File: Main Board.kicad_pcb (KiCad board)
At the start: 4 copper layers, 161 x 92 mm, 380 parts, among them J1 Motor Y, J10 CA58SUB-B, J11 PC6 EPSON MAINBOARD, J12 Y AXIS, J13 Z AXIS, J14 LED 1, J15 LED 2, J16 Power Input, J17 VS, J18 12V, J19 5V, J2 Motor Z, J20 3.3V, J21 TABLE SENSOR, J22 INPUT1, J23 INPUT2, J24 PHOTO SENSOR EMITER, J25 PHOTO SENSOR RECEIVER, J26 ANALOG, J27 INPUT3, J28 OUT1, J29 OUT2, J3 USB_B, J30 RELAY, J31 EMERGENCY, J32 EPSON POWER IN, J33 EPSON BOARD POWER, J34 Display, J35 SPI Interface, J36 I2C Interface, J37 LED4, J38 LED3, J39 Key 3, J4 SWD, J40 Key 4, J41 Key 1, J42 Key 2, J43 Encoder, J5 DEBUG, J6 LIMIT Y BACK, J7 LIMIT Y FRONT, J8 LIMIT Z UP, J9 LIMIT Z DOWN, K1 S13-24V-2C, Q1 2N7002K, Q10 2N7002K, Q11 BC817, Q12 BC817, Q13 BC817, Q14 2N7002K, Q15 2N7002K, Q16 2N7002K, Q17 BC817, Q18 2N7002K, Q19 2N7002K, Q2 2N7002K, Q20 2N7002K, Q21 2N7002K, Q3 2N7002K, Q4 2N7002K, Q5 2N7002K, Q6 2N7002K, Q7 2N7002K, Q8 YJS9435A, Q9 2N7002K, U1 TMC2209-LA, U10 74HC2G32, U11 74HC245, U12 SHTC3, U2 TMC2209-LA, U3 STM32F401VETx, U4 USBUF02W6, U5 74HC245, U6 MCP16301, U7 A4403, U8 MCP16301, U9 MCP6002-xSN, Y1 8MHz

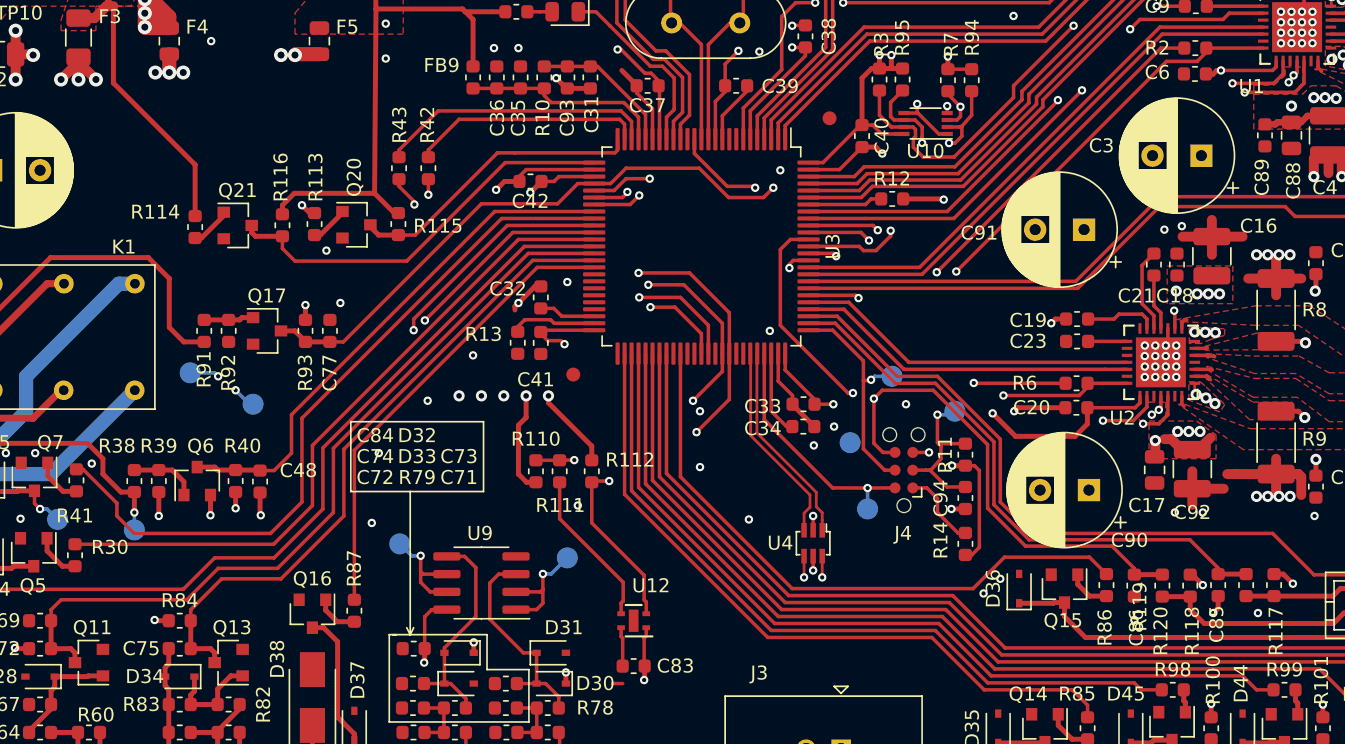
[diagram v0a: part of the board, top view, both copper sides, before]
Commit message: Added Nestimo logo, generated gerber files
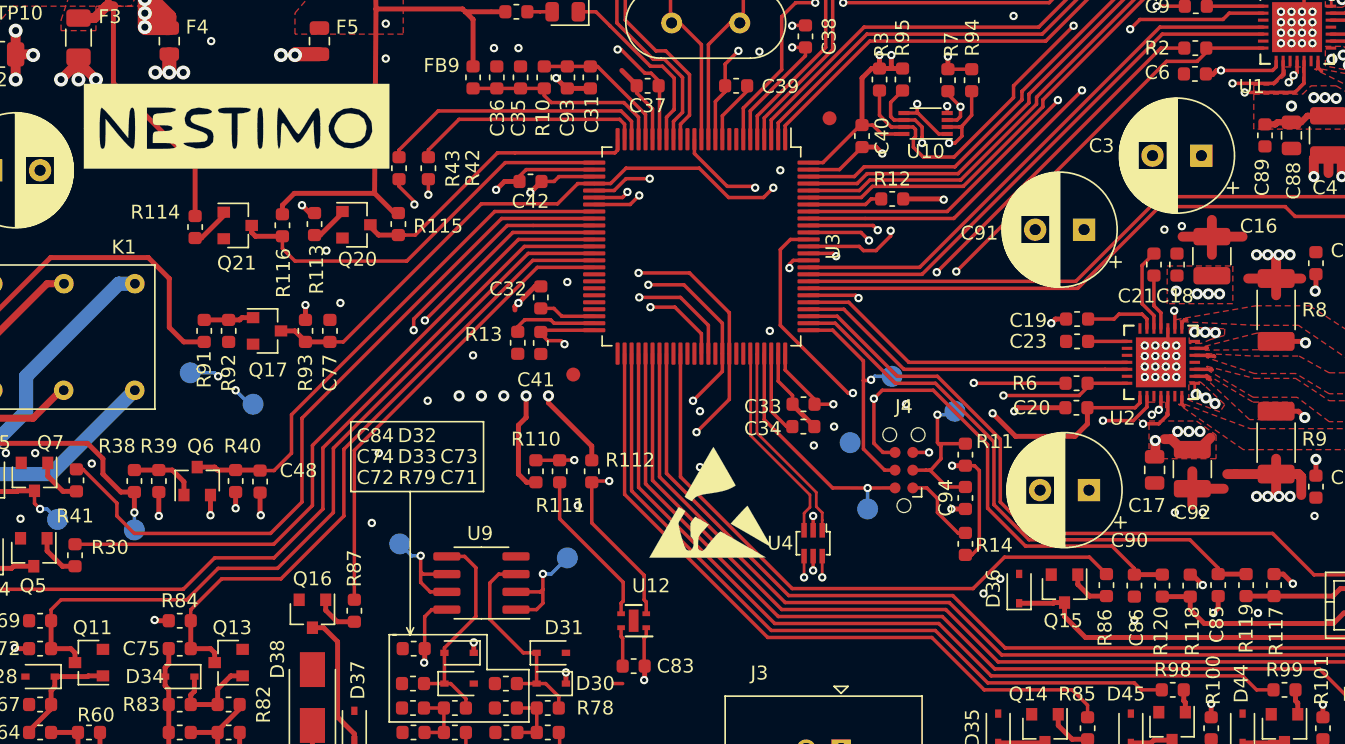
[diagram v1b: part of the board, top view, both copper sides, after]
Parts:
- added G***: LOGO, footprints:NESTIMO_logo_6.1mm, F.Cu at (89.2, 61.8)
- added REF**: ESD-Logo_8.9x8mm_SilkScreen, Symbol:ESD-Logo_8.9x8mm_SilkScreen, F.Cu at (123.2, 88.8)
- added REF**: WEEE-Logo_5.6x8mm_SilkScreen, Symbol:WEEE-Logo_5.6x8mm_SilkScreen, B.Cu at (145.2, 35.8)
- added REF**: RoHS-Logo_6mm_SilkScreen, Symbol:RoHS-Logo_6mm_SilkScreen, B.Cu at (166.2, 35.8)
- added REF**: CE-Logo_8.5x6mm_SilkScreen, Symbol:CE-Logo_8.5x6mm_SilkScreen, B.Cu at (186.2, 35.8)
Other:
- board text added: "Serial Number"

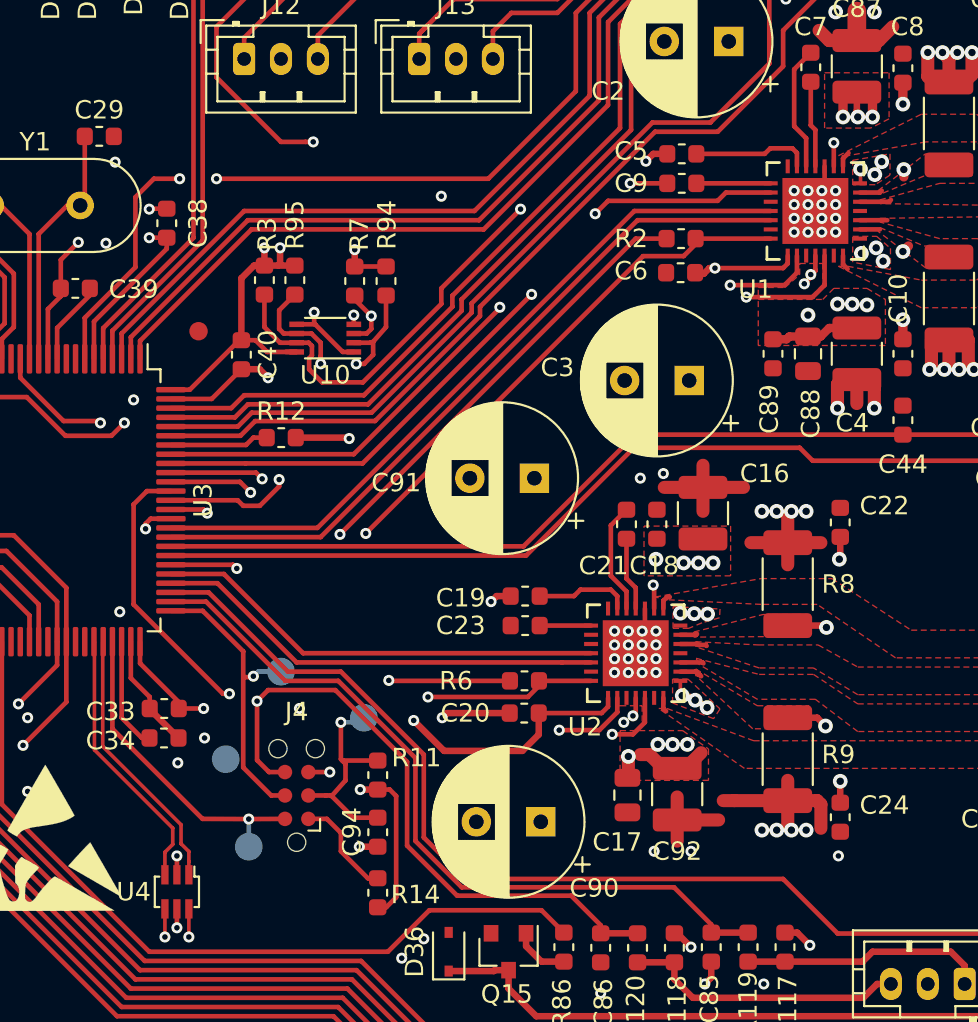
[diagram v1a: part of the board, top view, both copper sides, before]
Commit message: Added 3d packages, improved TMC2209 footprint
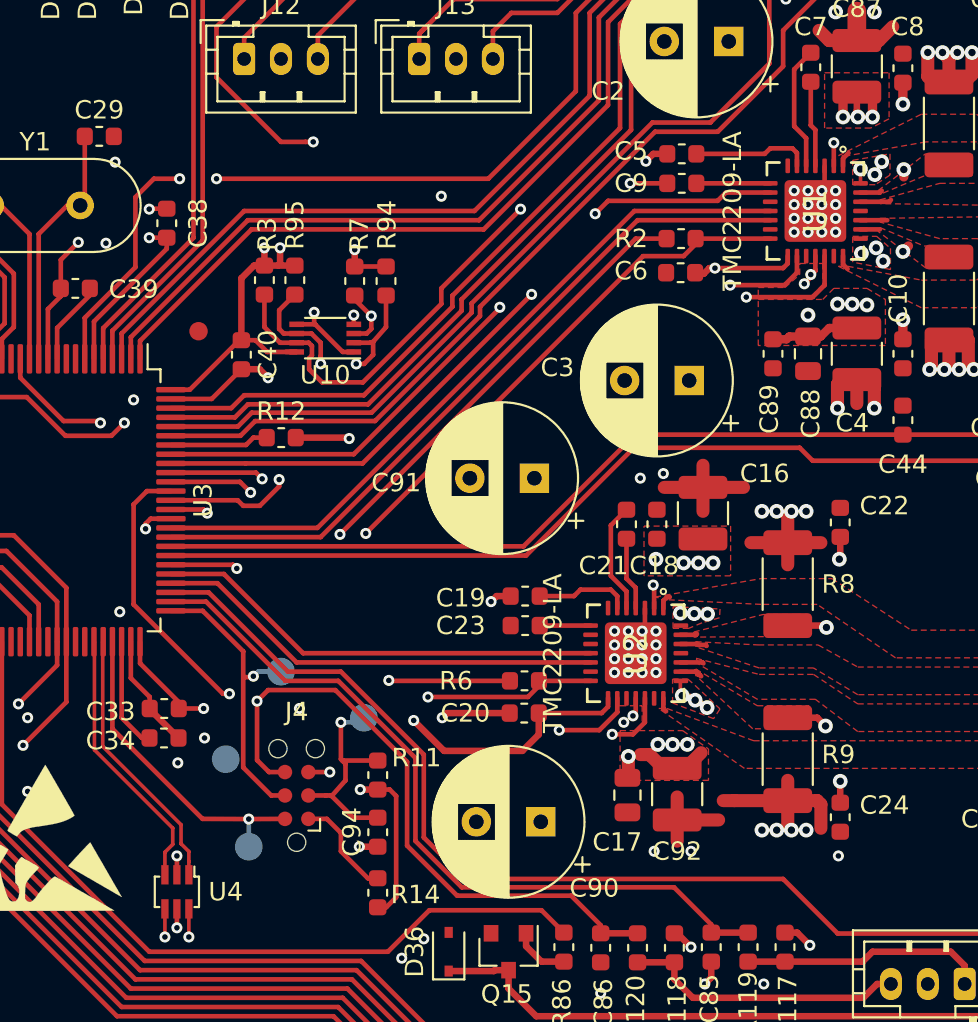
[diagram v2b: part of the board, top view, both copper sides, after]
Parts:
- U1, U2: footprint footprints:QFN-28_5X5_3X8_EPAD -> footprints:QFN-28_5X5mm_P0.5mm_EP3.35x.3.35mm

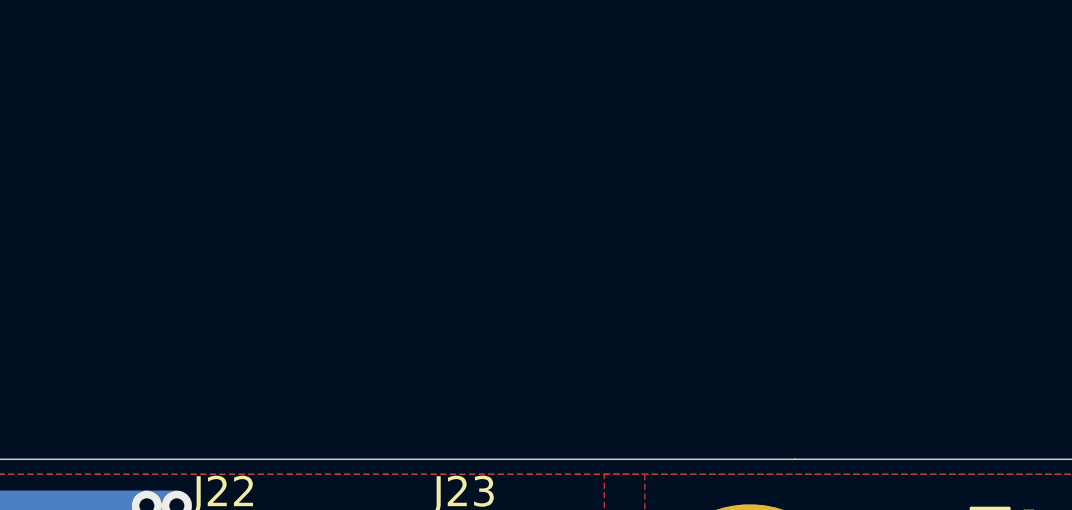
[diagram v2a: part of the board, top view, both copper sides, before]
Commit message: Added EEPROM on schematic
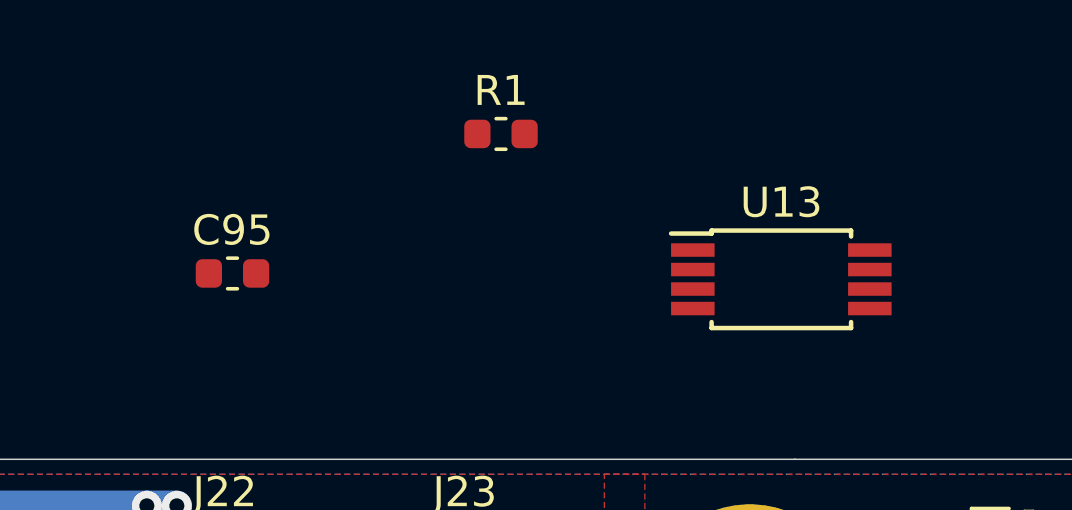
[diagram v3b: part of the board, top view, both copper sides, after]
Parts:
- added C95: 0.1uF, Capacitor_SMD:C_0603_1608Metric, F.Cu at (100.3, 17.8)
- added R1: 10kΩ, Resistor_SMD:R_0603_1608Metric, F.Cu at (109.2, 13.2)
- added U13: M24C02-WDW, Package_SO:TSSOP-8_4.4x3mm_P0.65mm, F.Cu at (118.5, 18.0)
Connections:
- U3 pad 62: Net-(U3-Pad62) -> EEPROM_P

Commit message: EEPROM Routing, Updated gerber files
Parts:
- moved U13 70.9 mm to (104.0, 87.4)
- moved R1 70.2 mm to (108.2, 83.3), turned to 270 degrees
- moved C95 65.9 mm to (106.5, 83.4), turned to 270 degrees
- turned R110 to 270 degrees
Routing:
- net EEPROM_P: track 0.00 -> 22.2 mm, vias 0 -> 2
- net I2C_SCL: track 83.3 -> 92.5 mm, vias 4 -> 5
- net +3V3: track 273.8 -> 279.5 mm
- net I2C_SDA: track 71.9 -> 76.9 mm
- net GND: vias 193 -> 196

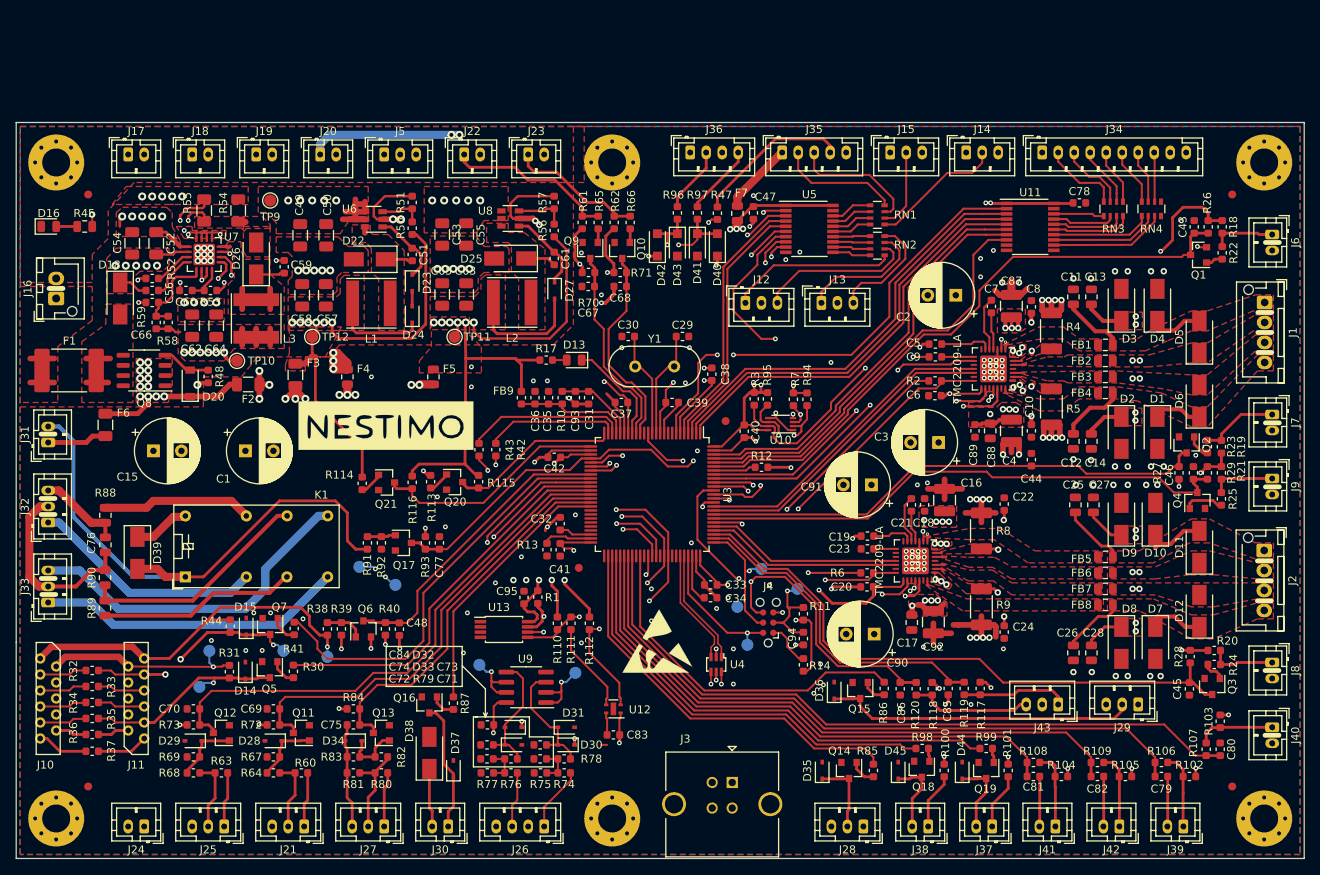
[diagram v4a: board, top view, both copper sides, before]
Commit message: Update silk layer, update TMC label, added revision, serial number, generated gerbera
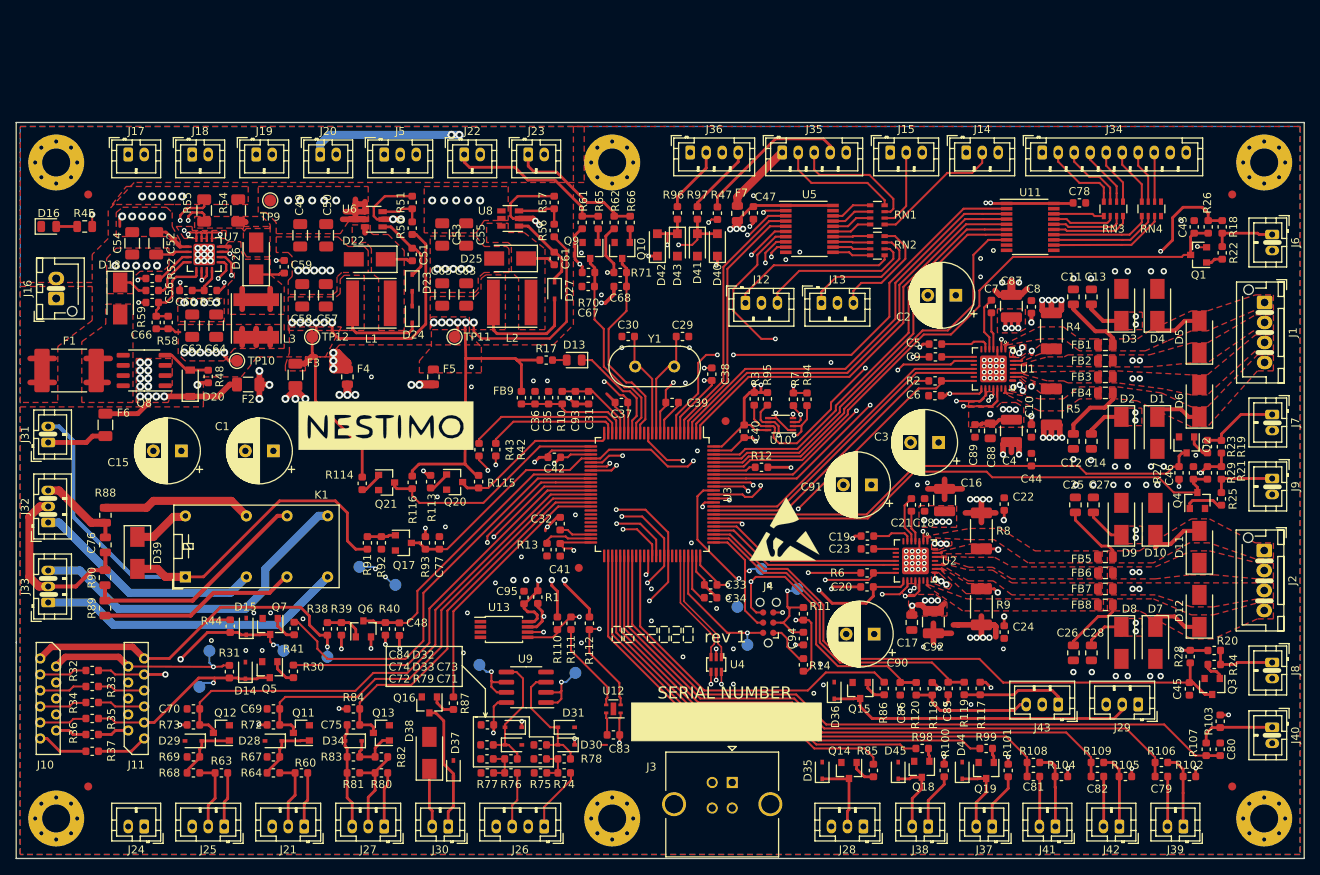
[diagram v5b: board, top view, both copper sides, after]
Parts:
- removed the REF** at (166.2, 35.8)
- removed the REF** at (186.2, 35.8)
- moved REF** 40.3 mm to (185.3, 38.2)
- moved REF** 21.2 mm to (139.1, 74.8)
- moved C1 3.50 mm to (75.2, 65.0), turned to 180 degrees
- moved C15 3.50 mm to (63.6, 65.0), turned to 180 degrees
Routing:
- added copper zone on In2.Cu, net VS
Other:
- board text added: "SERIAL NUMBER"
- board text added: "rev 1"
- board text removed: "Serial Number"
